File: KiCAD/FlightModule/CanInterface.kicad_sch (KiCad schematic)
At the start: 14 parts, among them U8 MCP2562-E-SN, U9 MCP2515-xST, Y1 8MHz

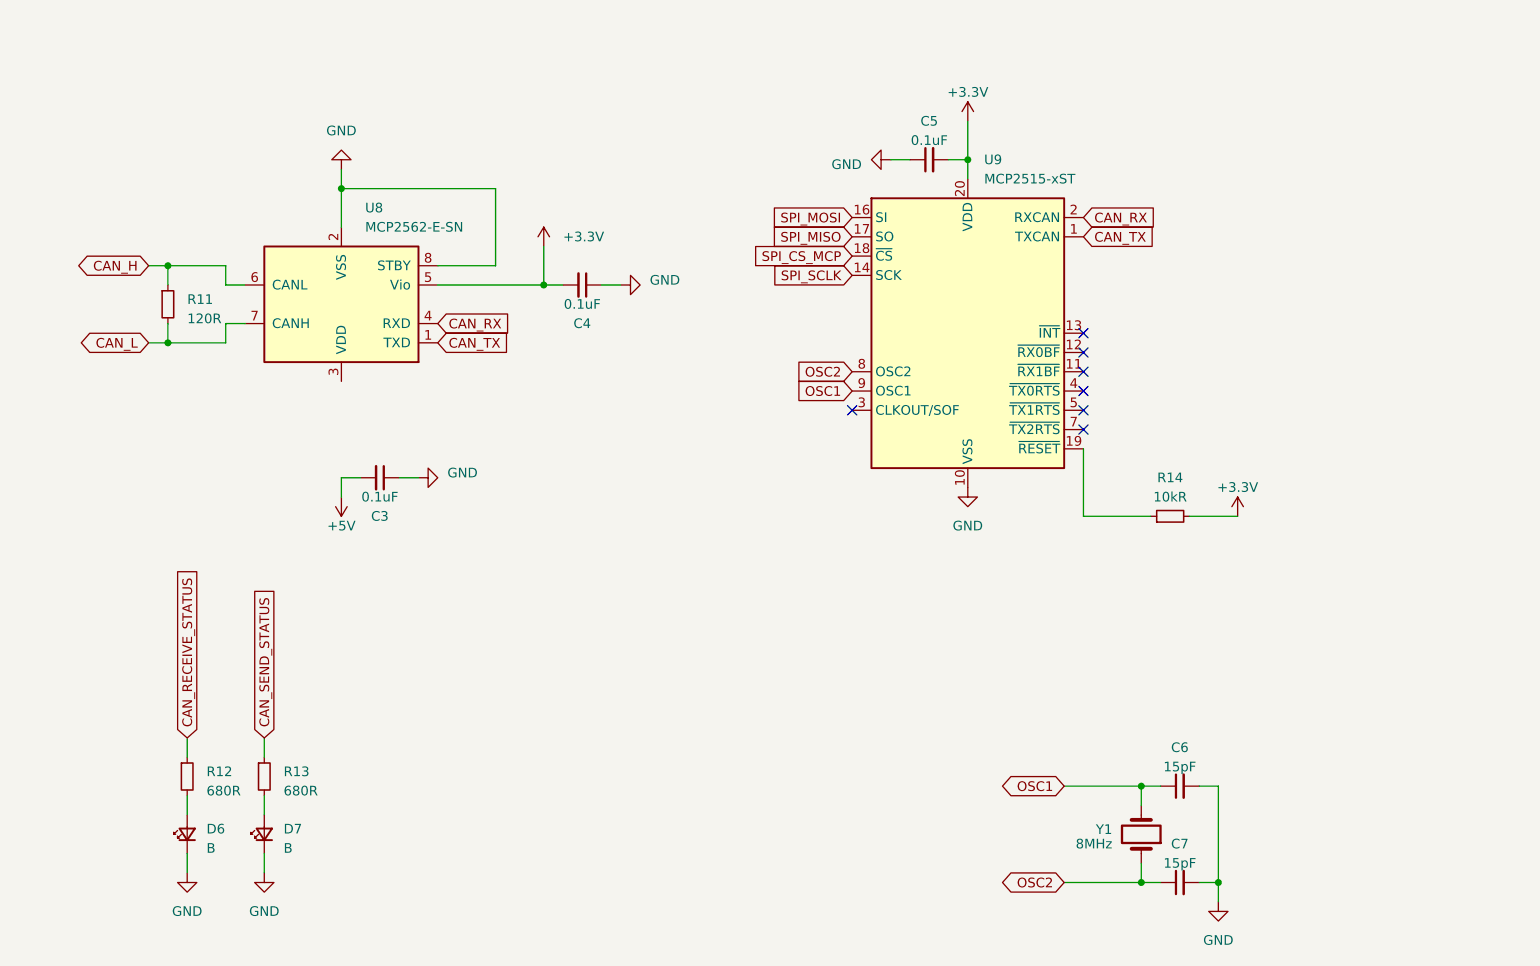
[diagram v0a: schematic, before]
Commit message: CANトランシーバーの配線完了
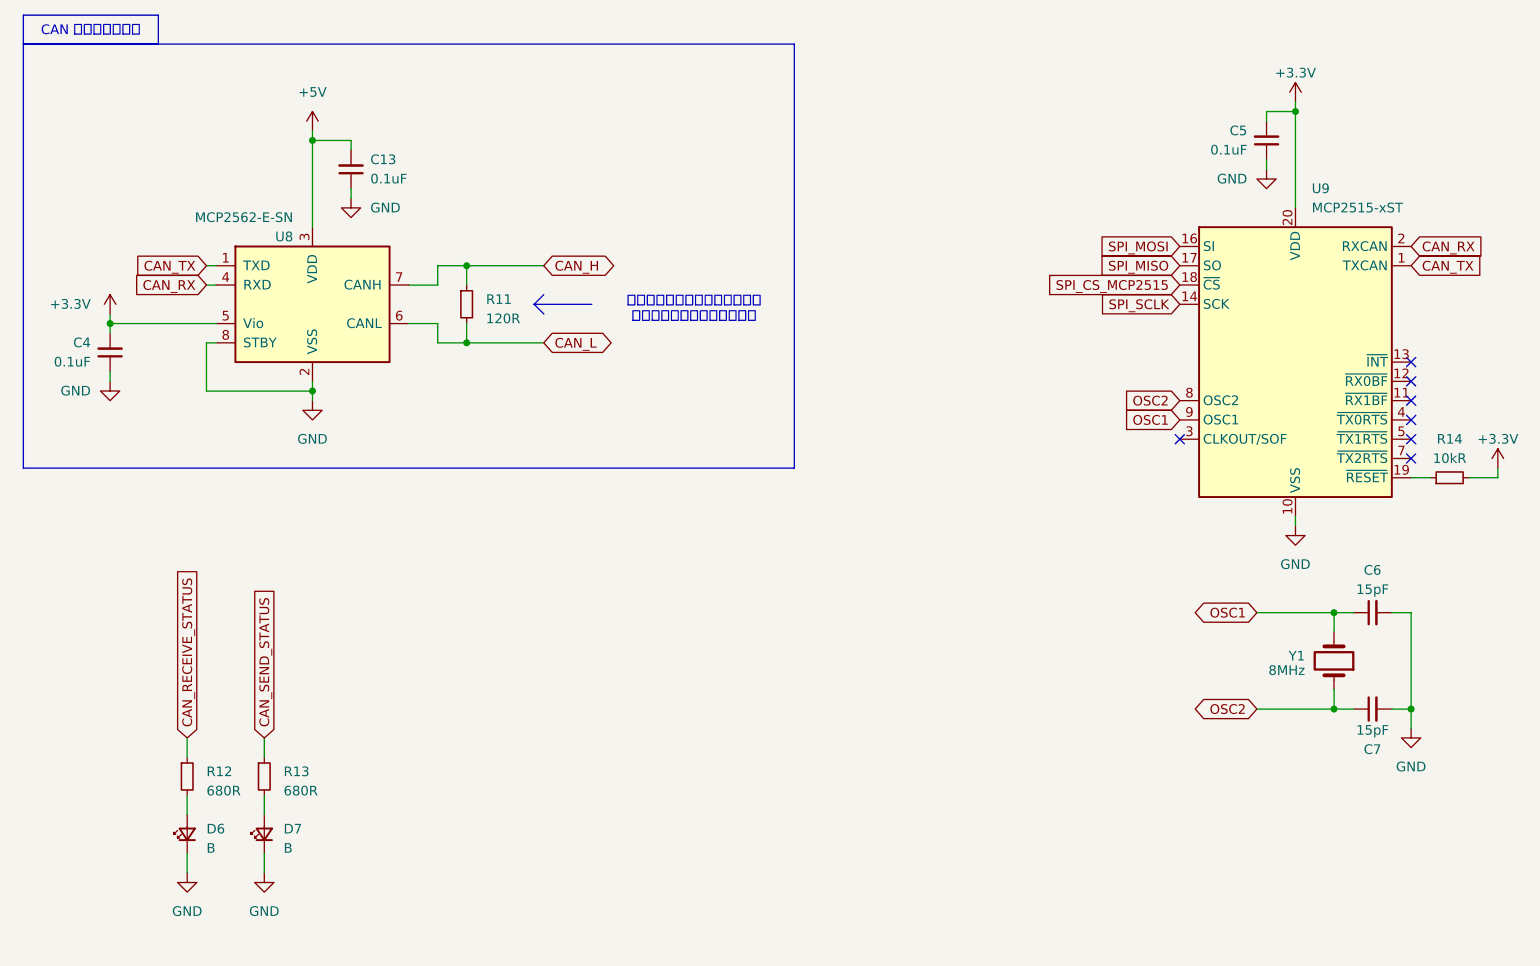
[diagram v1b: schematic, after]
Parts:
- removed C3: 0.1uF, Capacitor_SMD:C_0603_1608Metric_Pad1.08x0.95mm_HandSolder, symbol Device:C_Small
- added C13: 0.1uF, Capacitor_SMD:C_0603_1608Metric_Pad1.08x0.95mm_HandSolder, symbol Device:C_Small
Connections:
- net +5V: now also U8.3 (VDD), C13.2
- net CAN_H: now also U8.7 (CANH); no longer U8.6 (CANL)
- net CAN_L: now also U8.6 (CANL); no longer U8.7 (CANH)
- net GND: now also C13.1
- net SPI_CS_MCP renamed SPI_CS_MCP2515
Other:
- note added: "組み立て位置により終端抵抗の 取り付けを有無を決めること"
- moved on the sheet: C4, C5, C6, C7, R11, R14, U8, U9, Y1
